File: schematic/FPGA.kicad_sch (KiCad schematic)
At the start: 28 parts, among them J2 Flash, J3 SPI Select, U3 ICE5LP1K-SG48ITR, U4 AT25DN011-SSHF-T, U5 CCBTLV3257MPWREP, U6 TXS0108EPWR

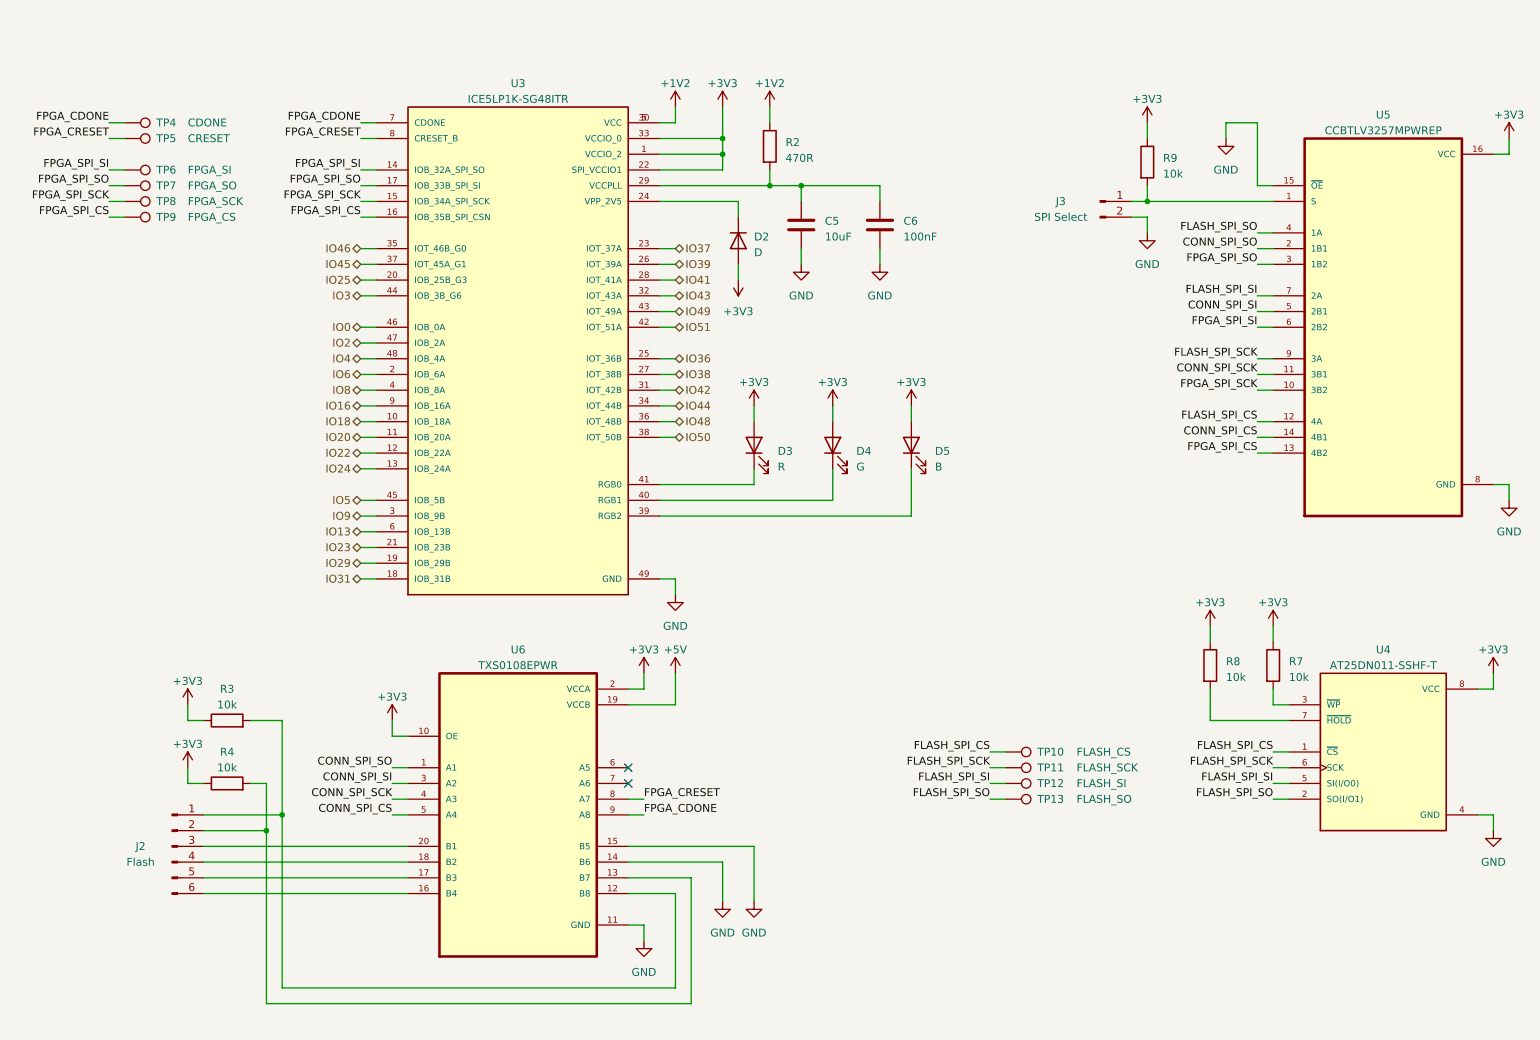
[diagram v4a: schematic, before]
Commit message: Update flash header schematic
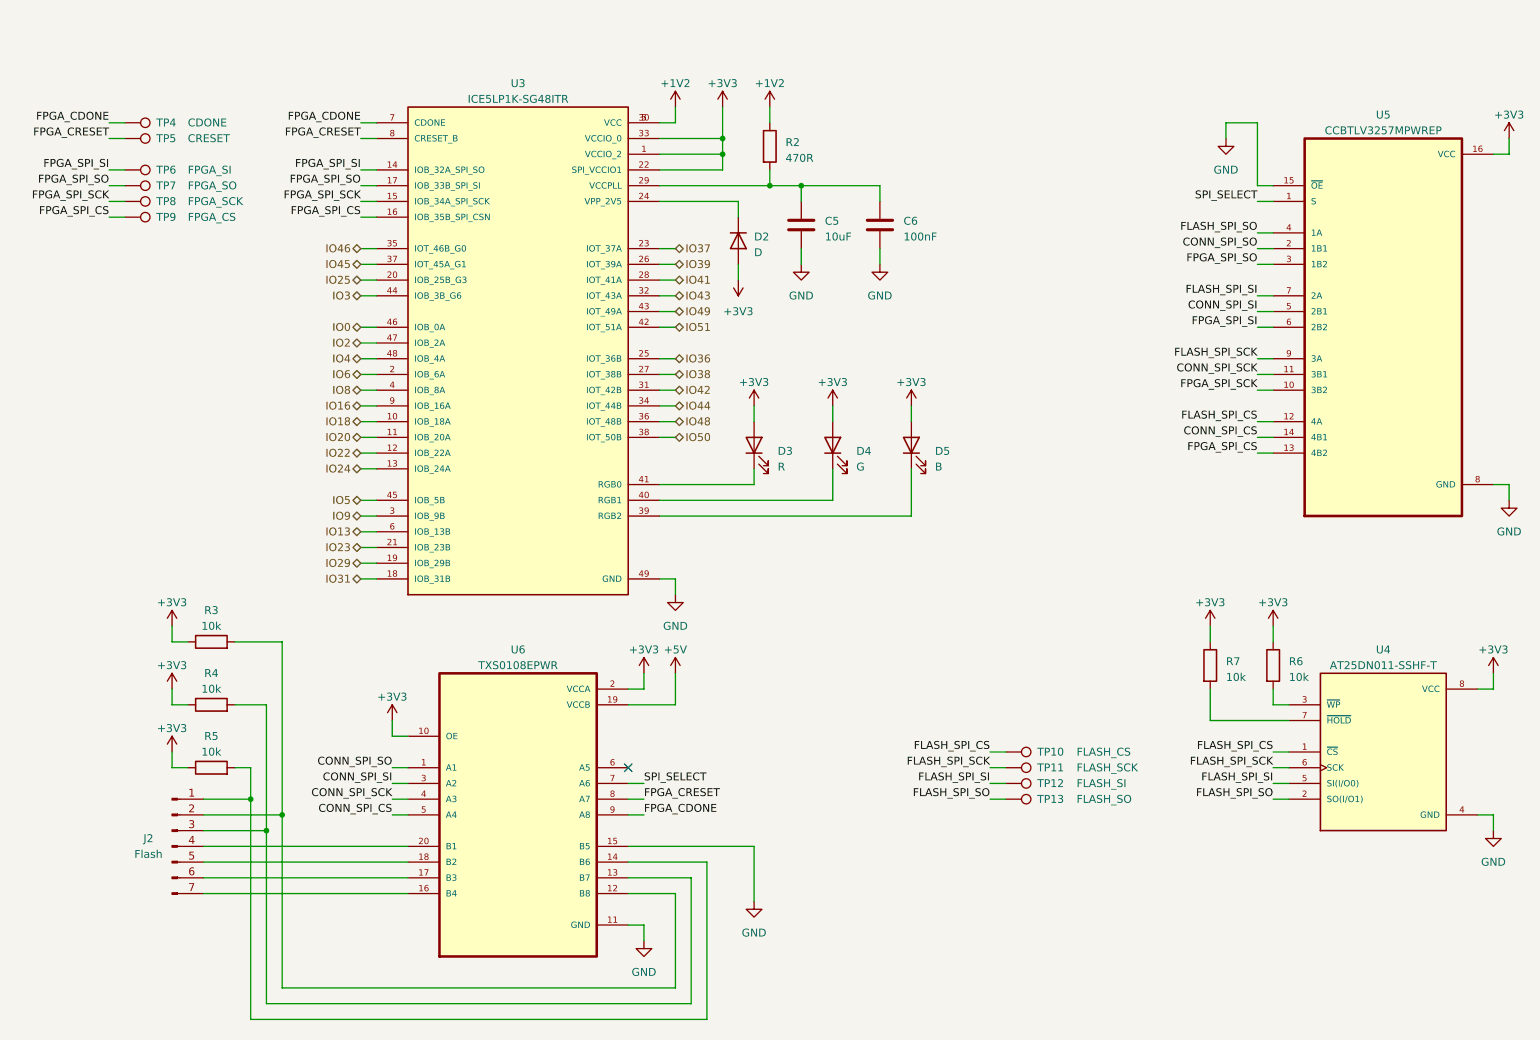
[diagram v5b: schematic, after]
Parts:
- removed J2: Flash, Connector_PinHeader_2.54mm:PinHeader_1x06_P2.54mm_Vertical, symbol Connector:Conn_01x06_Pin
- removed J3: SPI Select, Connector_PinHeader_2.54mm:PinHeader_1x02_P2.54mm_Vertical, symbol Connector:Conn_01x02_Pin
- removed R9: 10k, Resistor_SMD:R_0603_1608Metric, symbol Device:R
- added J2: Flash, Connector_PinHeader_2.54mm:PinHeader_1x07_P2.54mm_Vertical, symbol Connector:Conn_01x07_Pin
- added R5: 10k, Resistor_SMD:R_0603_1608Metric, symbol Device:R
- TP10, TP11, TP12, TP13, TP4, TP5, TP6, TP7, TP8, TP9: footprint TestPoint:TestPoint_Pad_D2.0mm -> TestPoint:TestPoint_Pad_D1.0mm
- U3: footprint ICE5LP1K-SG48ITR:QFN50P700X700X100-49N -> Package_DFN_QFN:QFN50P700X700X100-49N
- U4: footprint AT25DN011-SSHF-T:SOIC127P599X175-8N -> Package_SO:SOIC127P599X175-8N
- U5: footprint CCBTLV3257MPWREP:SOP65P640X120-16N -> Package_SO:SOP65P640X120-16N
- U6: footprint TXS0108EPWR:SOP65P640X120-20N -> Package_SO:SOP65P640X120-20N
- renumbered R7 to R6, R8 to R7
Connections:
- net +3V3: now also R5.1
- net GND: no longer U6.14 (B6)
- net at R4.2, U6.13 (B7): now also J2.3 (Pin_3)
- net SPI_SELECT: now reaches U5.1 (S)
- net SPI_SELECT: now also U6.7 (A6)
- net at R3.2, U6.12 (B8): now also J2.2 (Pin_2)
- net at U6.20 (B1): now also J2.4 (Pin_4)
- net at U6.18 (B2): now also J2.5 (Pin_5)
- net at U6.17 (B3): now also J2.6 (Pin_6)
- net at U6.16 (B4): now also J2.7 (Pin_7)
- new net: J2.1 (Pin_1), R5.2, U6.14 (B6)
- no-connect marks 2 -> 1
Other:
- moved on the sheet: R3, R4
